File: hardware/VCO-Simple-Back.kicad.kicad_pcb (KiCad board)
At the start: 2 copper layers, 29.2 x 97.8 mm, 86 parts, among them IC1 TL071, IC2 V3340SO16, IC3 LM397, IC4 TL072, IC5 TL072, P1 POWER_SIMPLE10_SHROUDED, Q1 3904, Q2 3904, U1 LM79L05A, U2 MC78L05A

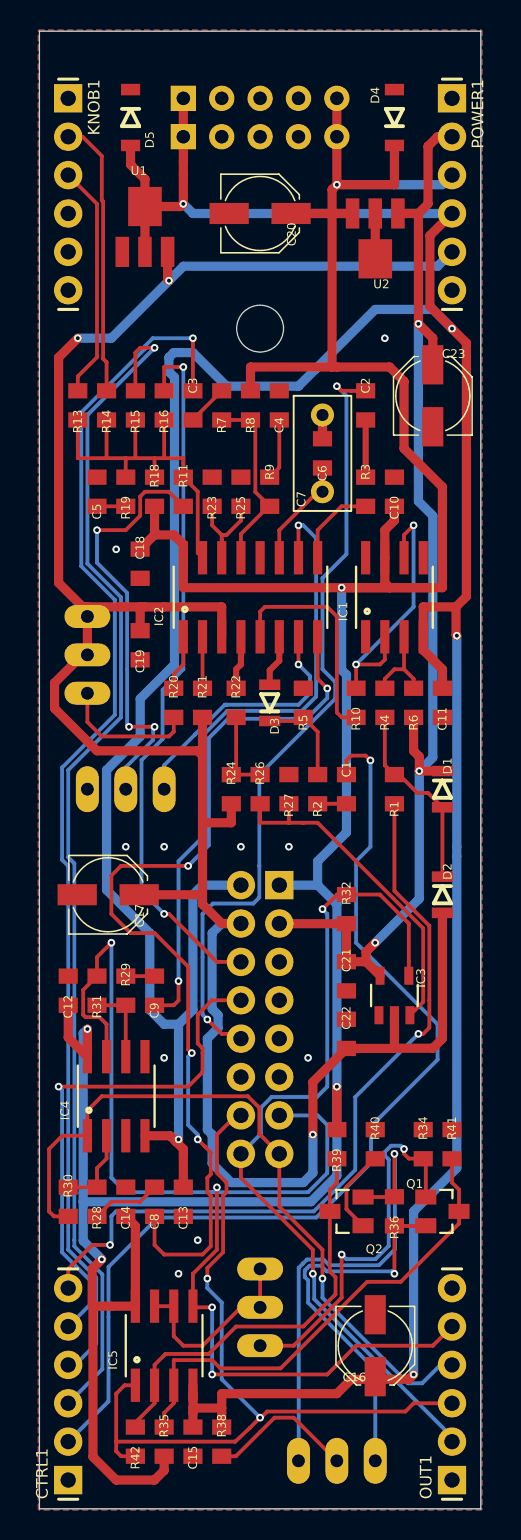
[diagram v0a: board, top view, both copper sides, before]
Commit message: silkscreen: move values to f-silk, added 3d models to footprints
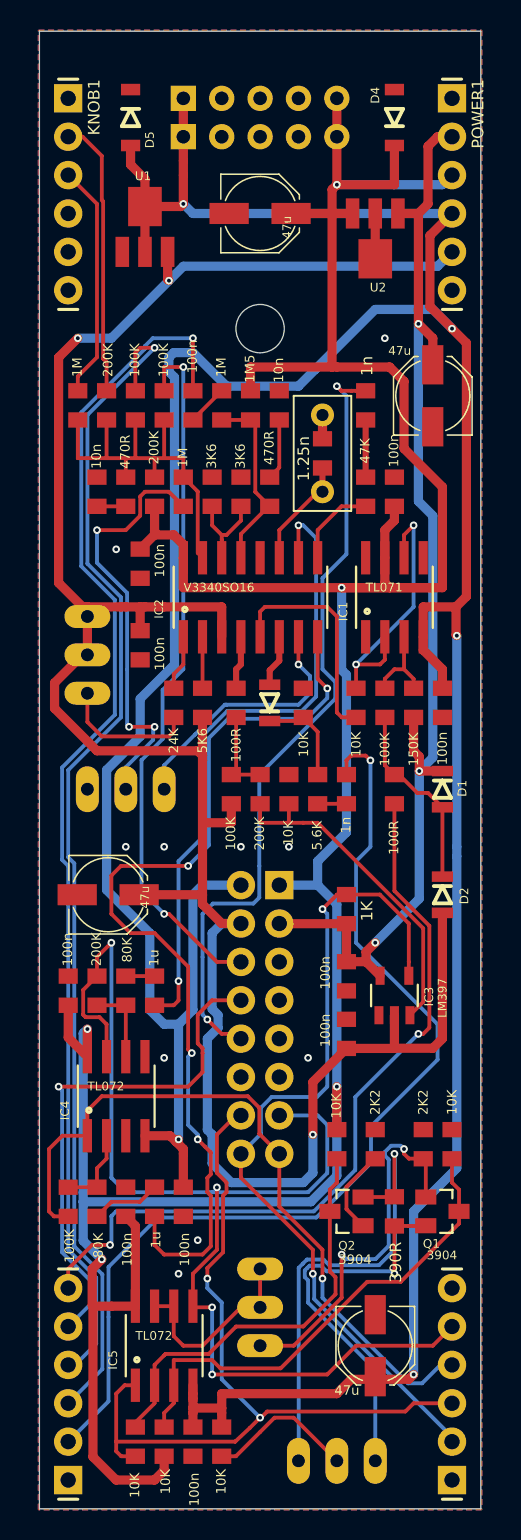
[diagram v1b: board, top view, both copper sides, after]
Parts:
- @HOLE0: value (none) -> MountingHole_3.2mm_M3; footprint (none) -> MountingHole:MountingHole_3.2mm_M3
- DRIVE1: value 100K -> (none)
- SYMMETRY1: value 50K -> (none)
